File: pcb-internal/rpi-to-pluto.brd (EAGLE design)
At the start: 77.8 x 29.2 mm, 7 parts, among them IC1 74HCT00, J1 JST-PH_4-PIN_HEADER

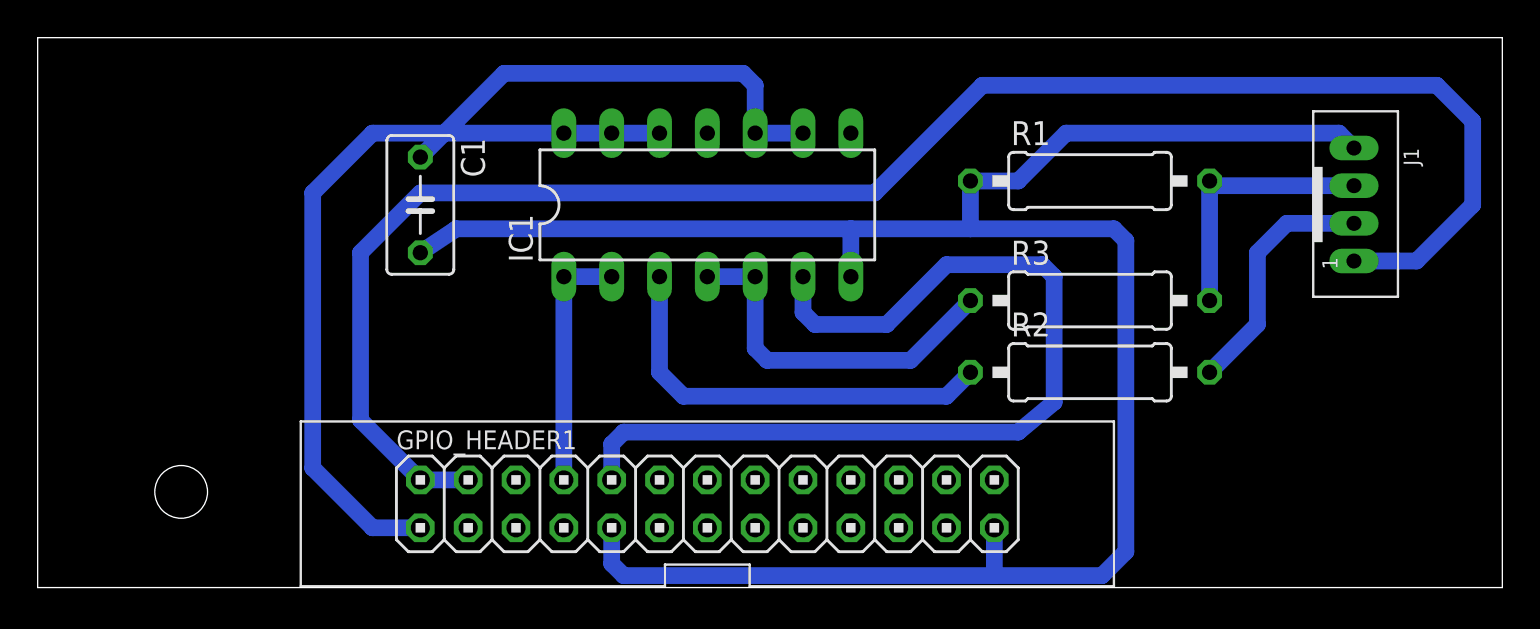
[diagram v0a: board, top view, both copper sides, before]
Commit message: New rpi-to-pluto board using the 74LVC2G14
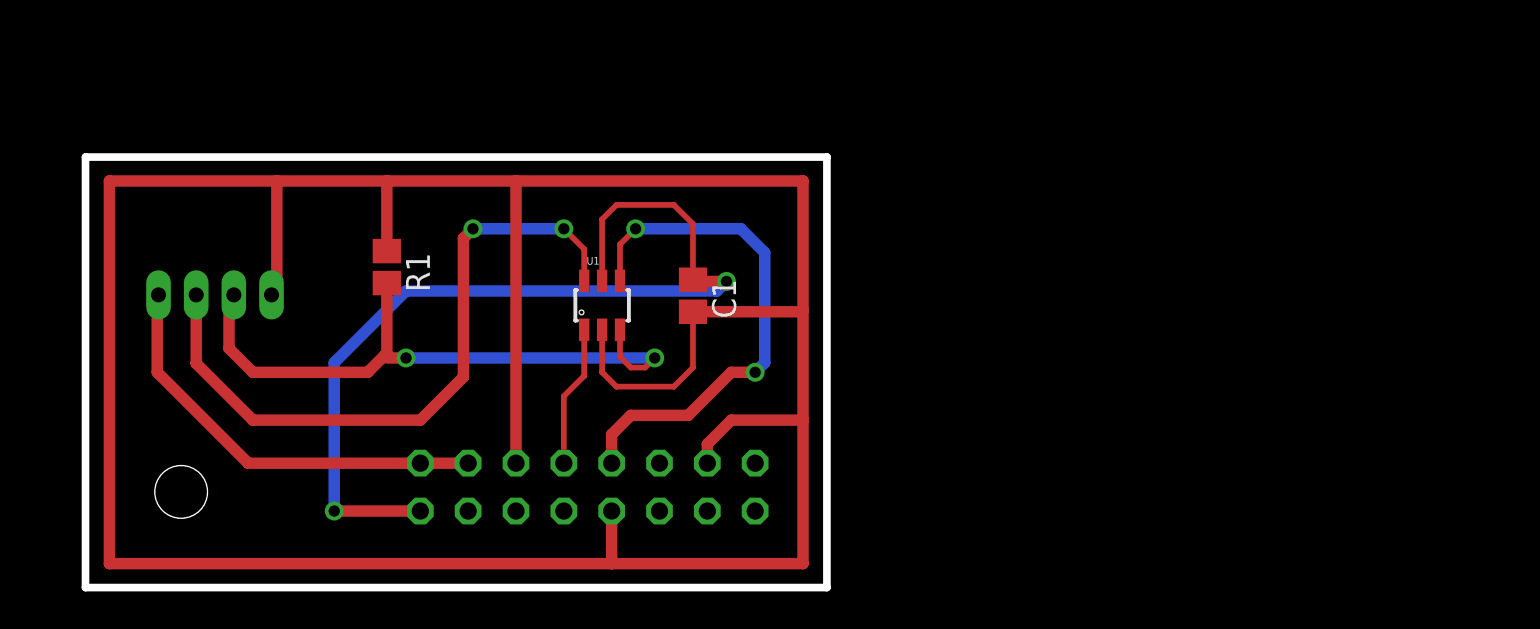
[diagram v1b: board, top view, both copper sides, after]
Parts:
- removed GPIO_HEADER1: RPI_GPIO_HEADER, rpi-header:2X13
- removed IC1: 74HCT00, 74xx-us:DIL14
- removed R2: 47, resistor:0309/12
- removed R3: 0, resistor:0309/12
- added SV1: (no value), con-lsta:FE08-2
- added U1: SN74LVC2G14DBV, lio:SOT23-6
- C1: value .1uF -> (none); device resistor:C050-035X075 -> resistor:C0805
- R1: value 4.7k -> 47K; device resistor:0309/12 -> resistor:R0805
- moved J1 60.6 mm to (9.40, 15.5), flipped to the bottom, turned to 0 degrees
- moved R1 37.6 mm to (18.5, 17.0), turned to 270 degrees
- moved C1 15.3 mm to (34.8, 15.5)
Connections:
- removed net N$1: J1.P3, R1.2, R3.2
- removed net N$2: IC1.3, R2.1
- removed net N$3: J1.P2, R2.2
- removed net N$4: GPIO_HEADER1.8, IC1.1, IC1.2
- removed net N$5: IC1.4, IC1.5, R3.1
- removed net N$7: GPIO_HEADER1.10, IC1.6
- new net FPGA_RXD: J1.P2, U1.6
- new net FPGA_TXD: J1.P3, R1.2, U1.3
- new net UART0_RXD: SV1.10, U1.4
- new net UART0_TXD: SV1.8, U1.1
- net +3V3: now also SV1.1, U1.5; no longer GPIO_HEADER1.1, GPIO_HEADER1.17, IC1.10, IC1.12, IC1.13, IC1.14, IC1.9
- net +5V: now also SV1.2, SV1.4; no longer GPIO_HEADER1.2, GPIO_HEADER1.4
- net GND: now also SV1.14, SV1.6, SV1.9, U1.2; no longer GPIO_HEADER1.14, GPIO_HEADER1.20, GPIO_HEADER1.25, GPIO_HEADER1.6, GPIO_HEADER1.9, IC1.7
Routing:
- net +5V: track 91.4 -> 22.6 mm
- net GND: track 114.0 -> 165.2 mm
- net N$7: track 50.0 -> 0.00 mm
- net FPGA_RXD: track 0.00 -> 36.1 mm, vias 0 -> 2
- net FPGA_TXD: track 0.00 -> 34.1 mm, vias 0 -> 2
- net UART0_RXD: track 0.00 -> 27.6 mm, vias 0 -> 2
- net N$2: track 22.6 -> 0.00 mm
- net N$5: track 19.4 -> 0.00 mm
- net +3V3: track 66.3 -> 48.7 mm, vias 0 -> 2
- net N$1: track 14.1 -> 0.00 mm
- net N$4: track 13.3 -> 0.00 mm
- net N$3: track 13.2 -> 0.00 mm
- net UART0_TXD: track 0.00 -> 7.53 mm
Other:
- board size 77.8 x 29.2 mm -> 39.4 x 22.9 mm
